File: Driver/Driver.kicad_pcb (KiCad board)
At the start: 4 copper layers, 65.5 x 90.8 mm, 97 parts, among them IC1 STM32G474RET6, IC2 ESDA6V1L, IC3 DRV8317HREER, J1 Conn_02x04_Top_Bottom, J2 ST-Link, J3 Encoder1, J4 Encoder2, J5 Jack-DC, J6 Screw_Terminal_01x03, J7 IMU, SW1 SW_Push, SW2 SW_Push, U1 LM2596S-ADJ, U2 LM2674M-5.0, U3 LD1117S33TR, Y2 TG2520SMN-32.0Mhz

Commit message: 1
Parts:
- moved L2 5.03 mm to (210.4, 69.1)
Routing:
- net +5V: track 163.4 -> 156.0 mm
- net Net-(D3-K): track 21.0 -> 16.3 mm
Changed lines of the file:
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@@
 	(footprint "SamacSys_Parts:LQH43MN470K03L"
 		(layer "F.Cu")
-		(at 205.5 70.25)
+		(at 210.4 69.1)
 		(descr "1812 (4532) L=4.5±0.3mm W=3.2±0.2mm T=2.6±0.2mm")
 		(tags "Inductor")
@@
 	)
 	(segment
-		(start 181.275 133.4875)
-		(end 181.2625 133.5)
-		(width 0.5)
-		(layer "F.Cu")
-		(net 3)
-	)
-	(segment
-		(start 213.2 69.6)
-		(end 213.2 65)
-		(width 0.65)
-		(layer "F.Cu")
-		(net 3)
-	)
-	(segment
-		(start 213.4 69.6)
-		(end 214.25 70.45)
+		(start 214.25 71.7)
+		(end 214.25 76.75)
 		(width 0.65)
 		(layer "F.Cu")
@@
 	)
 	(segment
-		(start 207 70.25)
-		(end 207 69.198)
-		(width 0.65)
+		(start 181.275 133.4875)
+		(end 181.2625 133.5)
+		(width 0.5)
 		(layer "F.Cu")
 		(net 3)
 	)
 	(segment
-		(start 207 70.25)
-		(end 207 71.05)
+		(start 211.9 70.152)
+		(end 212.848 71.1)
 		(width 0.65)
 		(layer "F.Cu")
@@
 	)
 	(segment
-		(start 197.9 73.3)
-		(end 197.9 72.3375)
+		(start 212.7 66.85)
+		(end 212.7 64.5)
 		(width 0.65)
 		(layer "F.Cu")
@@
 	)
 	(segment
-		(start 207.6 71.65)
-		(end 211.15 71.65)
+		(start 197.9 73.3)
+		(end 197.9 72.3375)
 		(width 0.65)
 		(layer "F.Cu")
@@
 	)
 	(segment
-		(start 207 71.05)
-		(end 207.6 71.65)
-		(width 0.65)
-		(layer "F.Cu")
-		(net 3)
-	)
-	(segment
 		(start 199.1625 72.3375)
 		(end 199.5 72)
@@
 	)
 	(segment
-		(start 213.2 69.6)
-		(end 213.4 69.6)
-		(width 0.65)
-		(layer "F.Cu")
-		(net 3)
-	)
-	(segment
 		(start 197.9 72.3375)
 		(end 199.1625 72.3375)
@@
 	)
 	(segment
-		(start 197.5 75)
-		(end 197.5 77)
+		(start 211.9 69.1)
+		(end 211.9 70.152)
 		(width 0.65)
 		(layer "F.Cu")
@@
 	)
 	(segment
-		(start 195.1 74.2)
-		(end 197 74.2)
+		(start 197.5 75)
+		(end 197.5 77)
 		(width 0.65)
 		(layer "F.Cu")
@@
 	)
 	(segment
-		(start 214.25 70.45)
-		(end 214.25 76.75)
+		(start 195.1 74.2)
+		(end 197 74.2)
 		(width 0.65)
 		(layer "F.Cu")
@@
 	)
 	(segment
-		(start 211.15 71.65)
-		(end 213.2 69.6)
+		(start 211.9 67.65)
+		(end 212.7 66.85)
+		(width 0.65)
+		(layer "F.Cu")
+		(net 3)
+	)
+	(segment
+		(start 211.9 69.1)
+		(end 211.9 67.65)
+		(width 0.65)
+		(layer "F.Cu")
+		(net 3)
+	)
+	(segment
+		(start 213.65 71.1)
+		(end 214.25 71.7)
+		(width 0.65)
+		(layer "F.Cu")
+		(net 3)
+	)
+	(segment
+		(start 212.848 71.1)
+		(end 213.65 71.1)
 		(width 0.65)
 		(layer "F.Cu")
@@
 	)
 	(segment
-		(start 207.6 68.1)
-		(end 205.05 68.1)
-		(width 0.65)
-		(layer "F.Cu")
-		(net 54)
-	)
-	(segment
-		(start 205.05 68.1)
-		(end 205 68.15)
-		(width 0.65)
-		(layer "F.Cu")
-		(net 54)
-	)
-	(segment
 		(start 208.5 63.6)
 		(end 208.4 63.6)
@@
 	)
 	(segment
-		(start 205 68.15)
-		(end 204.95 68.15)
-		(width 0.65)
-		(layer "F.Cu")
-		(net 54)
-	)
-	(segment
-		(start 204.95 68.15)
-		(end 204 69.1)
-		(width 0.65)
-		(layer "F.Cu")
-		(net 54)
-	)
-	(segment
-		(start 208.8 63.9)
-		(end 208.8 66.9)
-		(width 0.65)
-		(layer "F.Cu")
-		(net 54)
-	)
-	(segment
-		(start 204 69.1)
-		(end 204 70.25)
+		(start 203.59 62.3)
+		(end 203.295 62.005)
 		(width 0.65)
 		(layer "F.Cu")
@@
 	)
 	(segment
-		(start 203.59 62.3)
-		(end 203.295 62.005)
+		(start 208.9 64)
+		(end 208.9 69.1)
 		(width 0.65)
 		(layer "F.Cu")
@@
 	)
 	(segment
-		(start 208.8 66.9)
-		(end 207.6 68.1)
+		(start 208.8 63.9)
+		(end 208.9 64)
 		(width 0.65)
 		(layer "F.Cu")
@@
 		(polygon
 			(pts
-				(xy 178.9 114.65) (xy 173.1 114.65) (xy 173.1 114.65) (xy 171.5 114.65) (xy 171.5 115.25) (xy 178.9 115.25)
+				(xy 178.9 114.65) (xy 173.1 114.65) (xy 171.5 114.65) (xy 171.5 115.25) (xy 178.9 115.25)
 			)
 		)

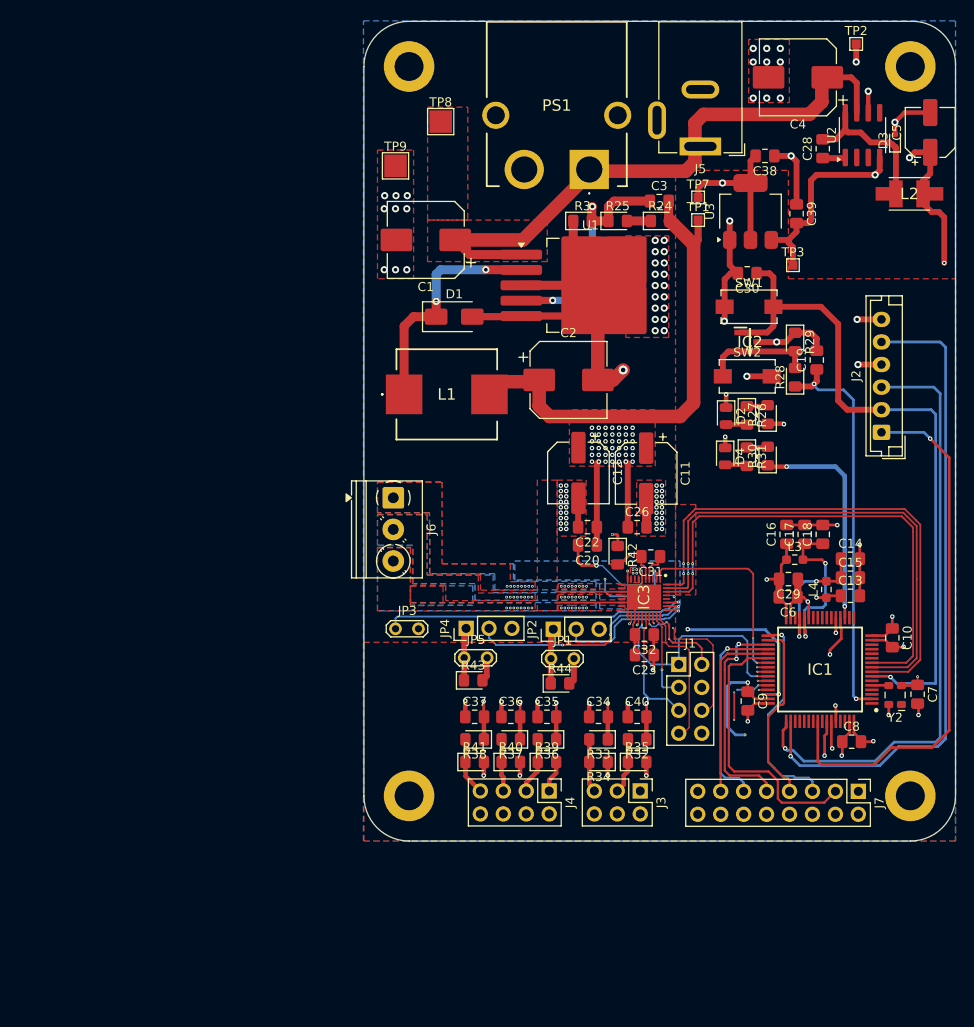
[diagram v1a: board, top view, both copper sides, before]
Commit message: Clear all Error in DRC
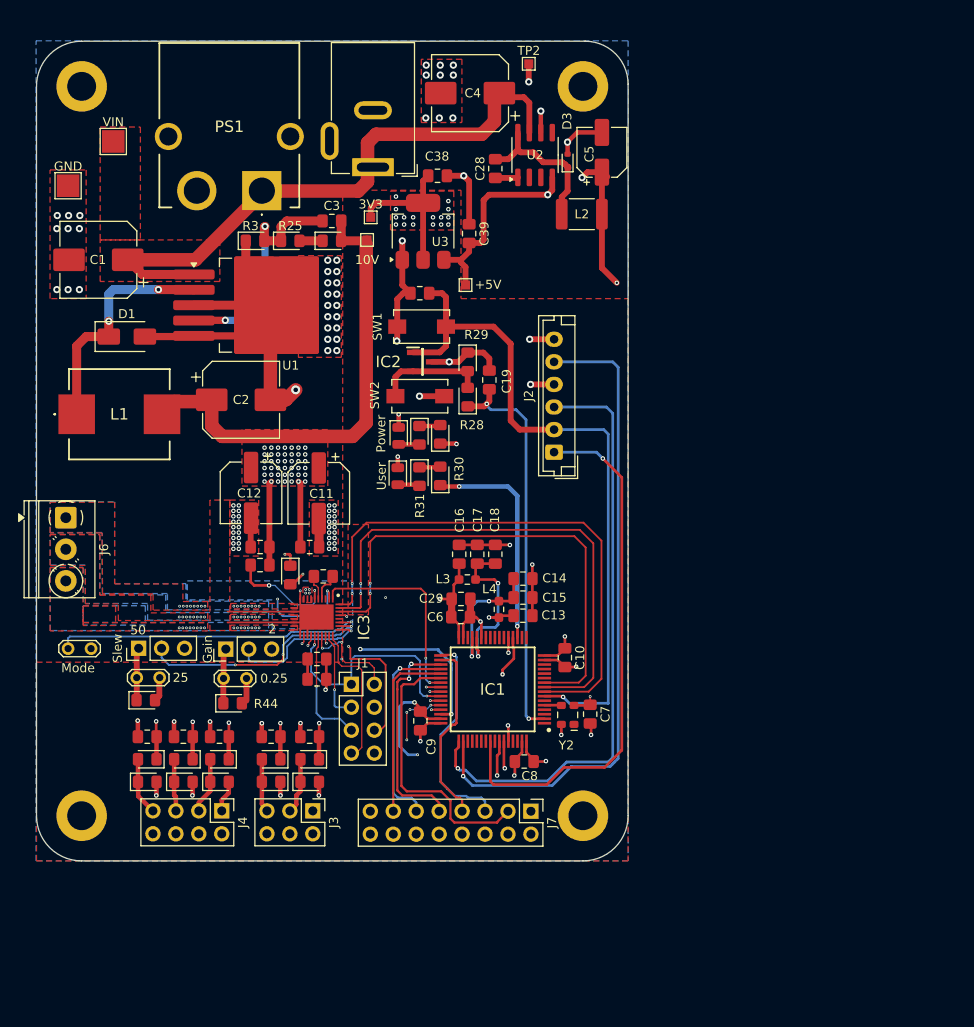
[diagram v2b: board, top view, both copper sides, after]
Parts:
- L2: footprint SamacSys_Parts:LQH43MN470K03L -> Inductor_SMD:L_1812_4532Metric_Pad1.30x3.40mm_HandSolder
- moved 10V 36.7 mm to (150.3, 74.2)
- moved R24 36.4 mm to (146.4, 74.3)
- moved C5 36.4 mm to (176.3, 64.5)
- moved C23 36.4 mm to (144.8, 122.8)
- moved C32 36.4 mm to (144.8, 120.6)
- moved L2 36.3 mm to (174.1, 71.3)
- moved C4 36.3 mm to (161.8, 58.0)
- moved PS1 36.3 mm to (138.7, 68.8)
- moved J5 36.3 mm to (151.0, 66.2)
- moved L1 36.3 mm to (122.9, 93.5)
- moved +5V 36.3 mm to (161.2, 79.2)
- moved 0.25 36.3 mm to (134.5, 122.8)
- moved 25 36.3 mm to (124.8, 122.7)
- moved 3V3 36.3 mm to (150.8, 71.7)
- moved C1 36.3 mm to (120.6, 76.4)
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- renumbered TP3 to +5V, JP1 to 0.25, TP1 to 10V, JP5 to 25, TP7 to 3V3, TP9 to GND, JP2 to Gain, JP3 to Mode, D2 to Power, JP4 to Slew, D4 to User, TP8 to VIN
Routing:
- net /3-Phase Driver/Vcurrfdbk_A: track 57.2 -> 60.0 mm
- net GND: track 180.7 -> 178.4 mm, vias 97 -> 98
- net VIN_AVDD: track 77.1 -> 75.5 mm
- net /3-Phase Driver/Vcurrfdbk_B: track 56.1 -> 57.4 mm
- net +5V: track 156.0 -> 154.9 mm
- net VDD: track 76.8 -> 76.2 mm, vias 17 -> 32
- net /3-Phase Driver/TIM1_CH2: track 40.9 -> 41.5 mm
- added copper zone on F.Cu, net VDD
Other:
- board size 65.5 x 90.8 mm -> 65.5 x 90.7 mm
- board text added: "2"
- board text added: "50"

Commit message: Add user Label
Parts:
- moved C31 0.59 mm to (146.1, 111.2)
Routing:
- net VDD: track 76.2 -> 74.9 mm
- net CPL: track 3.34 -> 4.23 mm
- net VIN_AVDD: vias 47 -> 81
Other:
- board text added: "A"
- board text added: "B"
- board text added: "C"
- board text added: "GND"
- board text added: "ST-LINK"

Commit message: 2
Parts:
- renumbered TP2 to GND, Power to PWR, SW1 to RESET, User to USER, SW2 to USER
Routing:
- net GND: track 178.4 -> 175.8 mm, vias 98 -> 109
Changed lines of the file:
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@@
 			(at 3.25 -0.05 270)
 			(layer "F.SilkS")
+			(hide yes)
 			(effects
 				(font
@@
 		(descr "LED SMD 0805 (2012 Metric), square (rectangular) end terminal, IPC_7351 nominal, (Body size source: https://docs.google.com/spreadsheets/d/1BsfQQcO9C6DZCsRaXUlFlo91Tg2WpOkGARC1WS5S8t0/edit?usp=sharing), generated with kicad-footprint-generator")
 		(tags "LED")
-		(property "Reference" "User"
-			(at -0.0125 1.8 90)
+		(property "Reference" "USER"
+			(at -0.0625 2.05 90)
 			(layer "F.SilkS")
 			(effects
@@
 		(at 156.3875 83.8)
 		(descr "Light Touch Switch, https://industrial.panasonic.com/cdbs/www-data/pdf/ATK0000/ATK0000CE7.pdf")
-		(property "Reference" "SW1"
-			(at -4.8875 0 90)
+		(property "Reference" "RESET"
+			(at -6.1375 0.1 180)
 			(layer "F.SilkS")
 			(effects
@@
 		(descr "LED SMD 0805 (2012 Metric), square (rectangular) end terminal, IPC_7351 nominal, (Body size source: https://docs.google.com/spreadsheets/d/1BsfQQcO9C6DZCsRaXUlFlo91Tg2WpOkGARC1WS5S8t0/edit?usp=sharing), generated with kicad-footprint-generator")
 		(tags "LED")
-		(property "Reference" "Power"
-			(at -0.25 1.95 90)
+		(property "Reference" "PWR"
+			(at -0.2 2 270)
 			(layer "F.SilkS")
 			(effects
@@
 			(at 0.775 2.1 270)
 			(layer "F.SilkS")
+			(hide yes)
 			(effects
 				(font
@@
 		(descr "SMD rectangular pad as test Point, square 1.0mm side length")
 		(tags "test point SMD pad rectangle square")
-		(property "Reference" "TP2"
-			(at 0 -1.448 0)
+		(property "Reference" "GND"
+			(at -0.05 -1.5 0)
 			(layer "F.SilkS")
 			(effects
@@
 		)
 		(fp_text user "${REFERENCE}"
-			(at 0 -1.45 0)
+			(at -0.05 -1.5 0)
 			(layer "F.Fab")
 			(effects
@@
 		(at 156.1875 91.5)
 		(descr "Light Touch Switch, https://industrial.panasonic.com/cdbs/www-data/pdf/ATK0000/ATK0000CE7.pdf")
-		(property "Reference" "SW2"
-			(at -4.9875 -0.1 90)
+		(property "Reference" "USER"
+			(at -6.0875 -0.1 180)
 			(layer "F.SilkS")
 			(effects
@@
 	)
 	(segment
-		(start 171.05 90.2)
-		(end 168.45 90.2)
-		(width 0.65)
-		(layer "F.Cu")
-		(net 96)
-	)
-	(segment
 		(start 172.25 121.4875)
 		(end 173.4625 121.4875)
@@
 	)
 	(via
-		(at 168.45 90.2)
-		(size 0.8)
-		(drill 0.4)
-		(layers "F.Cu" "B.Cu")
-		(net 96)
-	)
-	(via
 		(at 146.15 107.2)
 		(size 0.5)
@@
 	)
 	(via
+		(at 133.95 115.35)
+		(size 0.3)
+		(drill 0.15)
+		(layers "F.Cu" "B.Cu")
+		(net 96)
+	)
+	(via
 		(at 158.35 60.7)
 		(size 0.8)
@@
 	)
 	(via
+		(at 133.45 115.95)
+		(size 0.3)
+		(drill 0.15)
+		(layers "F.Cu" "B.Cu")
+		(free yes)
+		(net 96)
+	)
+	(via
 		(at 147 78.95)
 		(size 0.8)
@@
 	)
 	(via
+		(at 134.45 116.55)
+		(size 0.3)
+		(drill 0.15)
+		(layers "F.Cu" "B.Cu")
+		(net 96)
+	)
+	(via
 		(at 155.95 131.2)
 		(size 0.3)
@@
 	)
 	(via
+		(at 134.45 115.35)
+		(size 0.3)
+		(drill 0.15)
+		(layers "F.Cu" "B.Cu")
+		(net 96)
+	)
+	(via
 		(at 158.45 55.95)
 		(size 0.8)
@@
 	)
 	(via
+		(at 134.45 115.95)
+		(size 0.3)
+		(drill 0.15)
+		(layers "F.Cu" "B.Cu")
+		(free yes)
+		(net 96)
+	)
+	(via
 		(at 128.99211 127.524467)
 		(size 0.5)
@@
 	)
 	(via
+		(at 134.9 115.35)
+		(size 0.3)
+		(drill 0.15)
+		(layers "F.Cu" "B.Cu")
+		(net 96)
+	)
+	(via
 		(at 147 80.2)
 		(size 0.8)
@@
 	)
 	(via
+		(at 134.9 116.55)
+		(size 0.3)
+		(drill 0.15)
+		(layers "F.Cu" "B.Cu")
+		(net 96)
+	)
+	(via
 		(at 158.45 54.85)
 		(size 0.8)
@@
 	)
 	(via
+		(at 133.45 115.35)
+		(size 0.3)
+		(drill 0.15)
+		(layers "F.Cu" "B.Cu")
+		(net 96)
+	)
+	(via
 		(at 166.160052 107.97603)
 		(size 0.5)
@@
 	)
 	(via
+		(at 133.95 116.55)
+		(size 0.3)
+		(drill 0.15)
+		(layers "F.Cu" "B.Cu")
+		(net 96)
+	)
+	(via
 		(at 146 76.45)
 		(size 0.8)
@@
 	)
 	(via
+		(at 134.9 115.95)
+		(size 0.3)
+		(drill 0.15)
+		(layers "F.Cu" "B.Cu")
+		(free yes)
+		(net 96)
+	)
+	(via
 		(at 161.05 67.1)
 		(size 0.8)
@@
 	)
 	(via
+		(at 133.95 115.95)
+		(size 0.3)
+		(drill 0.15)
+		(layers "F.Cu" "B.Cu")
+		(free yes)
+		(net 96)
+	)
+	(via
 		(at 135.55 108.4)
 		(size 0.5)
@@
 		(net 96)
 	)
+	(via
+		(at 133.45 116.55)
+		(size 0.3)
+		(drill 0.15)
+		(layers "F.Cu" "B.Cu")
+		(net 96)
+	)

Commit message: 2
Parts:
- renumbered J1 to Debug
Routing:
- net V+: track 68.2 -> 69.2 mm
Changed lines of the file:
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@@
 		(descr "Through hole straight pin header, 2x04, 2.54mm pitch, double rows")
 		(tags "Through hole pin header THT 2x04 2.54mm double row")
-		(property "Reference" "J1"
-			(at 1.27 -2.33 0)
+		(property "Reference" "Debug"
+			(at 1.27 -2.45 0)
 			(layer "F.SilkS")
 			(effects
@@
 		(tags "capacitor electrolytic")
 		(property "Reference" "C4"
-			(at -0.3 0 0)
+			(at 0 0 0)
 			(layer "F.SilkS")
 			(effects
@@
 	)
 	(segment
-		(start 167.7 58.4)
-		(end 164.45 58.4)
-		(width 0.65)
+		(start 131.175 78.025)
+		(end 123.85 78.025)
+		(width 1)
 		(layer "F.Cu")
 		(net 57)
 	)
 	(segment
-		(start 131.175 78.025)
-		(end 125.475 78.025)
-		(width 1)
+		(start 167.7 58.4)
+		(end 164.45 58.4)
+		(width 0.65)
 		(layer "F.Cu")
 		(net 57)
@@
 	)
 	(segment
+		(start 123.85 78.025)
+		(end 123.85 76.4)
+		(width 1)
+		(layer "F.Cu")
+		(net 57)
+	)
+	(segment
 		(start 164.45 61.1)
 		(end 164.45 58.4)
@@
 	)
 	(segment
-		(start 125.475 78.025)
-		(end 123.85 76.4)
-		(width 1)
-		(layer "F.Cu")
-		(net 57)
-	)
-	(segment
 		(start 149.3625 68.7875)
 		(end 150.4 67.75)
@@
 		(polygon
 			(pts
-				(xy 156.35 54.2) (xy 156.35 61.2) (xy 160.85 61.2) (xy 160.85 54.2)
+				(xy 156.35 54.2) (xy 156.35 61.2) (xy 160.5 61.2) (xy 160.5 54.2)
 			)
 		)

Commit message: 2
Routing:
- net Net-(D3-K): track 16.8 -> 19.0 mm
- net /External Sensor and Encoder/Encoder1 B: track 47.5 -> 49.2 mm
- net /External Sensor and Encoder/Encoder1 A: track 42.5 -> 44.0 mm
- net /External Sensor and Encoder/Encoder2 B: track 46.9 -> 47.9 mm
- net V+: track 69.2 -> 68.2 mm
- net SWO: track 59.6 -> 60.4 mm
- net /External Sensor and Encoder/IMU_CS: track 31.0 -> 31.5 mm
- net +5V: track 154.9 -> 155.5 mm
- net GND: track 175.8 -> 176.3 mm, vias 109 -> 105
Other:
- board text removed: "GND"

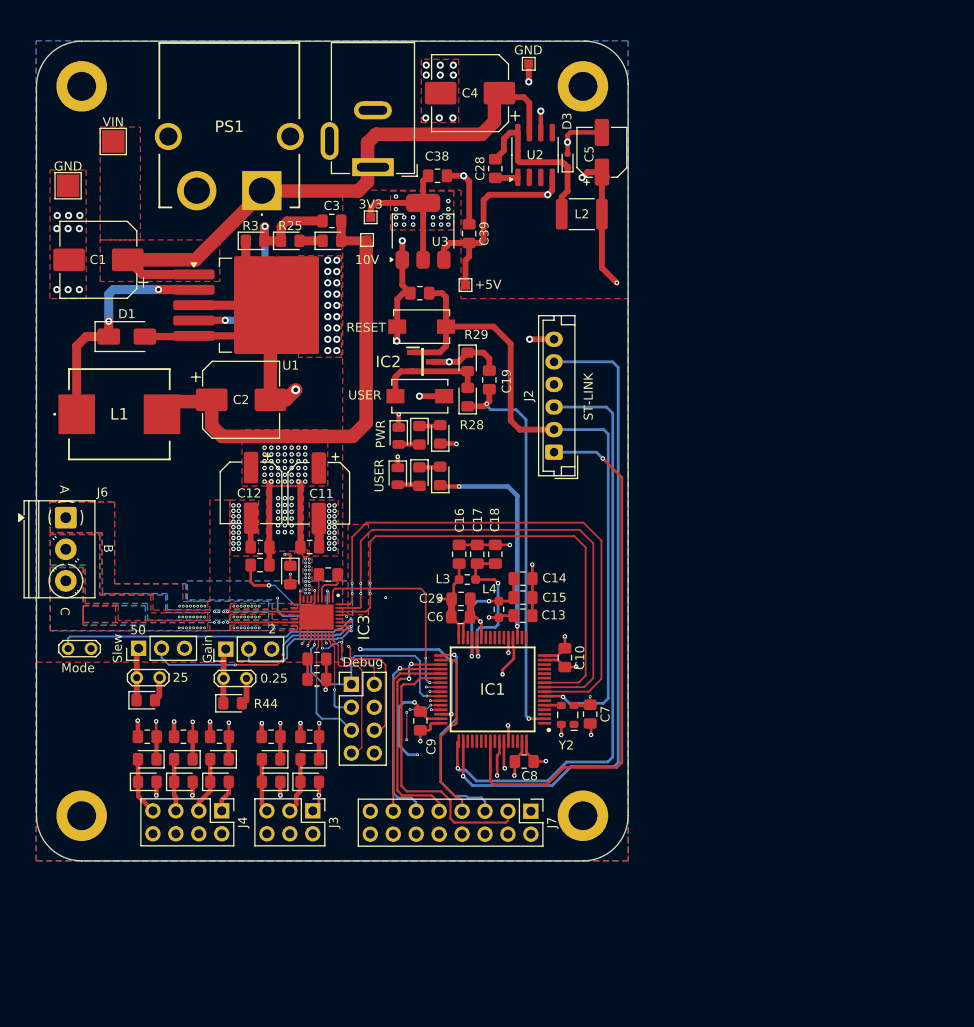
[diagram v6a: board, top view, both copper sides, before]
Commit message: Update a Connector and Trimpot
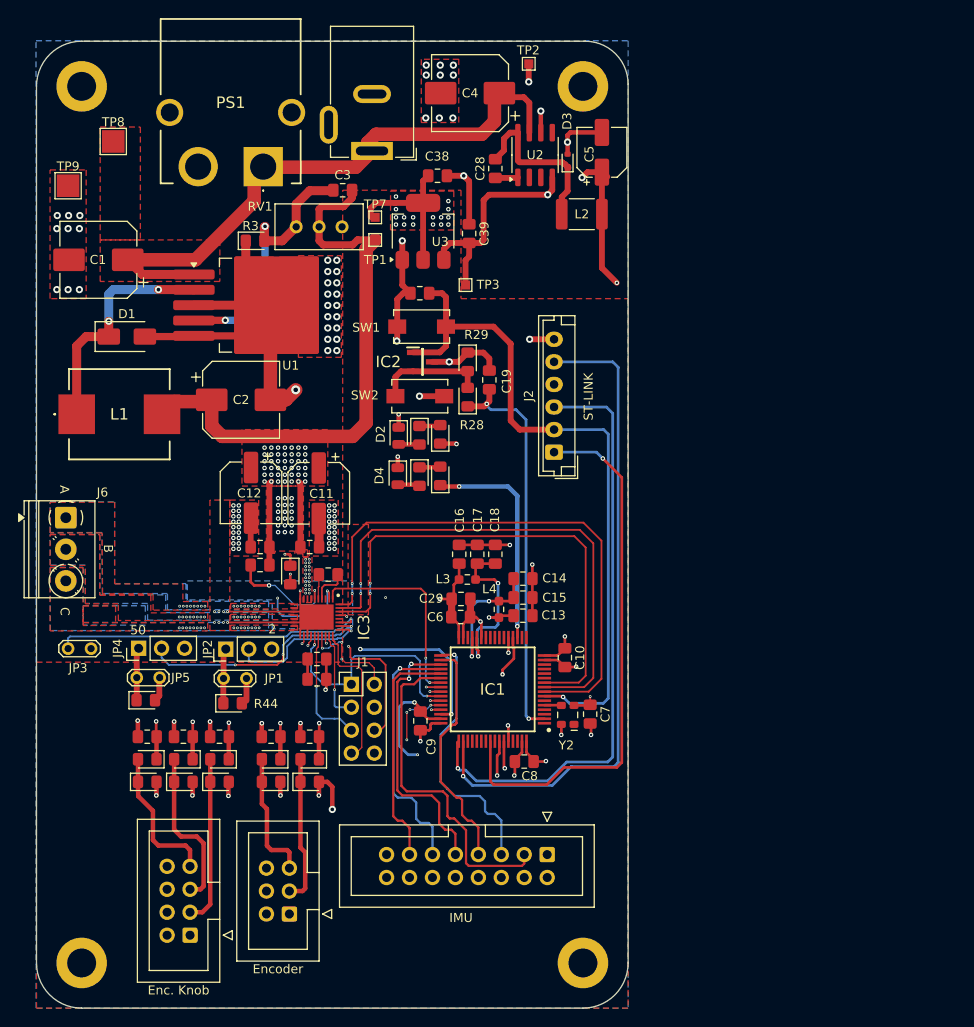
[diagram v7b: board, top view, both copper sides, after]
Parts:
- removed R24, R25: 3.6K, LED_SMD:LED_0805_2012Metric_Pad1.15x1.40mm_HandSolder
- added RV1: R_Potentiometer_Trim, Potentiometer_THT:Potentiometer_Bourns_3296W_Vertical, F.Cu at (142.5, 72.8)
- C1: value 330uF 50V -> 330uF 35V
- Enc. Knob: renamed from J4; footprint Connector_PinHeader_2.54mm:PinHeader_2x04_P2.54mm_Vertical -> Connector_IDC:IDC-Header_2x04_P2.54mm_Vertical
- Encoder: renamed from J3; footprint Connector_PinHeader_2.54mm:PinHeader_2x03_P2.54mm_Vertical -> Connector_IDC:IDC-Header_2x03_P2.54mm_Vertical
- IMU: renamed from J7; footprint Connector_PinHeader_2.54mm:PinHeader_2x08_P2.54mm_Vertical -> Connector_IDC:IDC-Header_2x08_P2.54mm_Vertical
- moved H2 16.3 mm to (118.8, 154.2)
- moved H3 16.3 mm to (174.2, 154.2)
- moved Enc. Knob 14.2 mm to (130.8, 151.2), turned to 180 degrees
- moved Encoder 11.7 mm to (141.8, 148.8), turned to 180 degrees
- moved IMU 5.13 mm to (170.3, 142.2)
- moved C3 3.61 mm to (147.7, 68.7)
- moved PS1 2.67 mm to (138.8, 66.1)
- moved J5 1.80 mm to (150.9, 64.3)
- moved TP1 0.90 mm to (151.2, 74.2)
- moved TP7 0.50 mm to (151.2, 71.7)
- renumbered PWR to D2, USER to D4, Debug to J1, 0.25 to JP1, Gain to JP2, Mode to JP3, Slew to JP4, 25 to JP5, RESET to SW1, USER to SW2, 10V to TP1, GND to TP2, +5V to TP3, 3V3 to TP7, VIN to TP8, GND to TP9
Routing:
- net Net-(J4-Pin_3): track 6.23 -> 18.7 mm
- net Net-(J4-Pin_5): track 5.79 -> 18.1 mm
- net VIN_AVDD: track 75.5 -> 86.5 mm
- net Net-(J3-Pin_3): track 6.20 -> 16.4 mm
- net Net-(J4-Pin_7): track 6.40 -> 16.0 mm
- net Net-(J3-Pin_5): track 5.94 -> 14.3 mm
- net /External Sensor and Encoder/IMU_MISO: track 22.6 -> 28.7 mm
- net /External Sensor and Encoder/IMU_CS: track 31.5 -> 37.6 mm
- net /External Sensor and Encoder/IMU_INT2: track 23.3 -> 29.3 mm
- net /External Sensor and Encoder/IMU_SCLK: track 24.6 -> 30.6 mm
- net /External Sensor and Encoder/IMU_MOSI: track 20.1 -> 25.9 mm
- net /External Sensor and Encoder/IMU_INT1: track 20.4 -> 26.2 mm
- net Net-(U1-FB): track 27.1 -> 30.9 mm
- net +5V: track 155.5 -> 158.0 mm, vias 5 -> 6
- net VDD: track 75.1 -> 73.1 mm, vias 32 -> 33
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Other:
- board size 65.5 x 90.7 mm -> 65.5 x 107 mm

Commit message: Update
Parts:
- removed SW1, SW2: SW_Push, Button_Switch_SMD:SW_SPST_EVQPE1
- added RESET: SW_Push, Button_Switch_SMD:SW_Tactile_SPST_NO_Straight_CK_PTS636Sx25SMTRLFS, F.Cu at (155.6, 83.5)
- added USER: SW_Push, Button_Switch_SMD:SW_Tactile_SPST_NO_Straight_CK_PTS636Sx25SMTRLFS, F.Cu at (155.7, 91.9)
- Encoder Knob: renamed from Enc. Knob
- IMU : renamed from IMU
- moved PA5 0.54 mm to (153.8, 100.9)
- moved R27 0.54 mm to (158.5, 96.3)
- moved PWR 0.54 mm to (153.9, 96.4)
- moved R30 0.54 mm to (158.5, 100.9)
- moved R26 0.54 mm to (156.2, 96.4)
- moved R31 0.54 mm to (156.2, 100.9)
- renumbered JP2 to Gain, JP3 to Mode, D4 to PA5, D2 to PWR, JP4 to Slew
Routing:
- net Net-(IC2-K2): track 12.3 -> 14.0 mm
- net GND: track 176.3 -> 175.6 mm, vias 105 -> 104
- net VDD: track 73.1 -> 73.7 mm
- net LED: track 24.7 -> 24.2 mm
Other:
- board text added: "R43"
